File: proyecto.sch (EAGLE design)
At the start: 0 parts

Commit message: Avance :)
.
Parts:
- added IC1: ADE9153AACPZ, SamacSys_Parts:ADE9153AACPZ
- added J1: 796638-3, SamacSys_Parts:796638-3
- added K1: PR28-3V-360-1A-E, PR28-3V-360-1A-E:PR28-3V-360-1A-E
- added PS1: RAC03-3.3SK, SamacSys_Parts:RAC03-3.3SK
- added U1: ESP32-PICO-MINI-02-N8R2ESP32-PICO-MINI-02_EXP, 2024-09-07_16-09-34_Library:ESP32-PICO-MINI-02-N8R2ESP32-PICO-MINI-02_EXP
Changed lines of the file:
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@@
 <setting verticaltext="up"/>
 </settings>
-<grid distance="0.1" unitdist="inch" unit="inch" style="lines" multiple="1" display="yes" altdistance="0.01" altunitdist="inch" altunit="inch"/>
+<grid distance="0.1" unitdist="inch" unit="inch" style="lines" multiple="1" display="no" altdistance="0.01" altunitdist="inch" altunit="inch"/>
 <layers>
+<layer number="1" name="Top" color="4" fill="1" visible="no" active="no"/>
+<layer number="2" name="Route2" color="1" fill="3" visible="no" active="no"/>
+<layer number="3" name="Route3" color="4" fill="3" visible="no" active="no"/>
+<layer number="4" name="Route4" color="1" fill="4" visible="no" active="no"/>
+<layer number="5" name="Route5" color="4" fill="4" visible="no" active="no"/>
+<layer number="6" name="Route6" color="1" fill="8" visible="no" active="no"/>
+<layer number="7" name="Route7" color="4" fill="8" visible="no" active="no"/>
+<layer number="8" name="Route8" color="1" fill="2" visible="no" active="no"/>
+<layer number="9" name="Route9" color="4" fill="2" visible="no" active="no"/>
+<layer number="10" name="Route10" color="1" fill="7" visible="no" active="no"/>
+<layer number="11" name="Route11" color="4" fill="7" visible="no" active="no"/>
+<layer number="12" name="Route12" color="1" fill="5" visible="no" active="no"/>
+<layer number="13" name="Route13" color="4" fill="5" visible="no" active="no"/>
+<layer number="14" name="Route14" color="1" fill="6" visible="no" active="no"/>
+<layer number="15" name="Route15" color="4" fill="6" visible="no" active="no"/>
+<layer number="16" name="Bottom" color="1" fill="1" visible="no" active="no"/>
+<layer number="17" name="Pads" color="2" fill="1" visible="no" active="no"/>
+<layer number="18" name="Vias" color="2" fill="1" visible="no" active="no"/>
+<layer number="19" name="Unrouted" color="6" fill="1" visible="no" active="no"/>
+<layer number="20" name="Dimension" color="15" fill="1" visible="no" active="no"/>
+<layer number="21" name="tPlace" color="7" fill="1" visible="no" active="no"/>
+<layer number="22" name="bPlace" color="7" fill="1" visible="no" active="no"/>
+<layer number="23" name="tOrigins" color="15" fill="1" visible="no" active="no"/>
+<layer number="24" name="bOrigins" color="15" fill="1" visible="no" active="no"/>
+<layer number="25" name="tNames" color="7" fill="1" visible="no" active="no"/>
+<layer number="26" name="bNames" color="7" fill="1" visible="no" active="no"/>
+<layer number="27" name="tValues" color="7" fill="1" visible="no" active="no"/>
+<layer number="28" name="bValues" color="7" fill="1" visible="no" active="no"/>
+<layer number="29" name="tStop" color="7" fill="3" visible="no" active="no"/>
+<layer number="30" name="bStop" color="7" fill="6" visible="no" active="no"/>
+<layer number="31" name="tCream" color="7" fill="4" visible="no" active="no"/>
+<layer number="32" name="bCream" color="7" fill="5" visible="no" active="no"/>
+<layer number="33" name="tFinish" color="6" fill="3" visible="no" active="no"/>
+<layer number="34" name="bFinish" color="6" fill="6" visible="no" active="no"/>
+<layer number="35" name="tGlue" color="7" fill="4" visible="no" active="no"/>
+<layer number="36" name="bGlue" color="7" fill="5" visible="no" active="no"/>
+<layer number="37" name="tTest" color="7" fill="1" visible="no" active="no"/>
+<layer number="38" name="bTest" color="7" fill="1" visible="no" active="no"/>
+<layer number="39" name="tKeepout" color="4" fill="11" visible="no" active="no"/>
+<layer number="40" name="bKeepout" color="1" fill="11" visible="no" active="no"/>
+<layer number="41" name="tRestrict" color="4" fill="10" visible="no" active="no"/>
+<layer number="42" name="bRestrict" color="1" fill="10" visible="no" active="no"/>
+<layer number="43" name="vRestrict" color="2" fill="10" visible="no" active="no"/>
+<layer number="44" name="Drills" color="7" fill="1" visible="no" active="no"/>
+<layer number="45" name="Holes" color="7" fill="1" visible="no" active="no"/>
+<layer number="46" name="Milling" color="3" fill="1" visible="no" active="no"/>
+<layer number="47" name="Measures" color="7" fill="1" visible="no" active="no"/>
+<layer number="48" name="Document" color="7" fill="1" visible="no" active="no"/>
+<layer number="49" name="Reference" color="7" fill="1" visible="no" active="no"/>
+<layer number="51" name="tDocu" color="7" fill="1" visible="no" active="no"/>
+<layer number="52" name="bDocu" color="7" fill="1" visible="no" active="no"/>
 <layer number="88" name="SimResults" color="9" fill="1" visible="yes" active="yes"/>
 <layer number="89" name="SimProbes" color="9" fill="1" visible="yes" active="yes"/>
@@
 <parts>
 <part name="FRAME1" library="frames" library_urn="urn:adsk.eagle:library:229" deviceset="A4L-LOC" device=""/>
+<part name="J1" library="SamacSys_Parts" deviceset="796638-3" device=""/>
+<part name="PS1" library="SamacSys_Parts" deviceset="RAC03-3.3SK" device=""/>
+<part name="K1" library="PR28-3V-360-1A-E" deviceset="PR28-3V-360-1A-E" device=""/>
+<part name="FRAME2" library="frames" library_urn="urn:adsk.eagle:library:229" deviceset="A4L-LOC" device=""/>
+<part name="U1" library="2024-09-07_16-09-34_Library" deviceset="ESP32-PICO-MINI-02-N8R2" device="ESP32-PICO-MINI-02_EXP"/>
+<part name="IC1" library="SamacSys_Parts" deviceset="ADE9153AACPZ" device=""/>
 </parts>
 <sheets>
@@
 <attribute name="SHEET" x="230.505" y="5.08" size="2.54" layer="94"/>
 </instance>
+<instance part="J1" gate="G$1" x="33.02" y="149.86" smashed="yes">
+<attribute name="NAME" x="49.53" y="157.48" size="1.778" layer="95" align="center-left"/>
+<attribute name="VALUE" x="49.53" y="154.94" size="1.778" layer="96" align="center-left"/>
+</instance>
+<instance part="PS1" gate="G$1" x="27.94" y="116.84" smashed="yes">
+<attribute name="NAME" x="62.23" y="124.46" size="1.778" layer="95" align="center-left"/>
+<attribute name="VALUE" x="62.23" y="121.92" size="1.778" layer="96" align="center-left"/>
+</instance>
+<instance part="K1" gate="G$1" x="363.22" y="121.92" smashed="yes">
+<attribute name="NAME" x="355.6" y="128.27" size="1.778" layer="95"/>
+<attribute name="VALUE" x="355.6" y="114.3" size="1.778" layer="96"/>
+</instance>
+<instance part="FRAME2" gate="G$1" x="269.24" y="0" smashed="yes">
+<attribute name="DRAWING_NAME" x="486.41" y="15.24" size="2.54" layer="94"/>
+<attribute name="LAST_DATE_TIME" x="486.41" y="10.16" size="2.286" layer="94"/>
+<attribute name="SHEET" x="499.745" y="5.08" size="2.54" layer="94"/>
+</instance>
+<instance part="U1" gate="A" x="109.22" y="142.24" smashed="yes">
+<attribute name="NAME" x="124.8146" y="151.3586" size="2.083" layer="95" ratio="6"/>
+<attribute name="VALUE" x="124.1752" y="148.8186" size="2.083" layer="96" ratio="6"/>
+</instance>
+<instance part="IC1" gate="G$1" x="401.32" y="106.68" smashed="yes">
+<attribute name="NAME" x="433.07" y="134.62" size="1.778" layer="95" align="center-left"/>
+<attribute name="VALUE" x="433.07" y="132.08" size="1.778" layer="96" align="center-left"/>
+</instance>
 </instances>

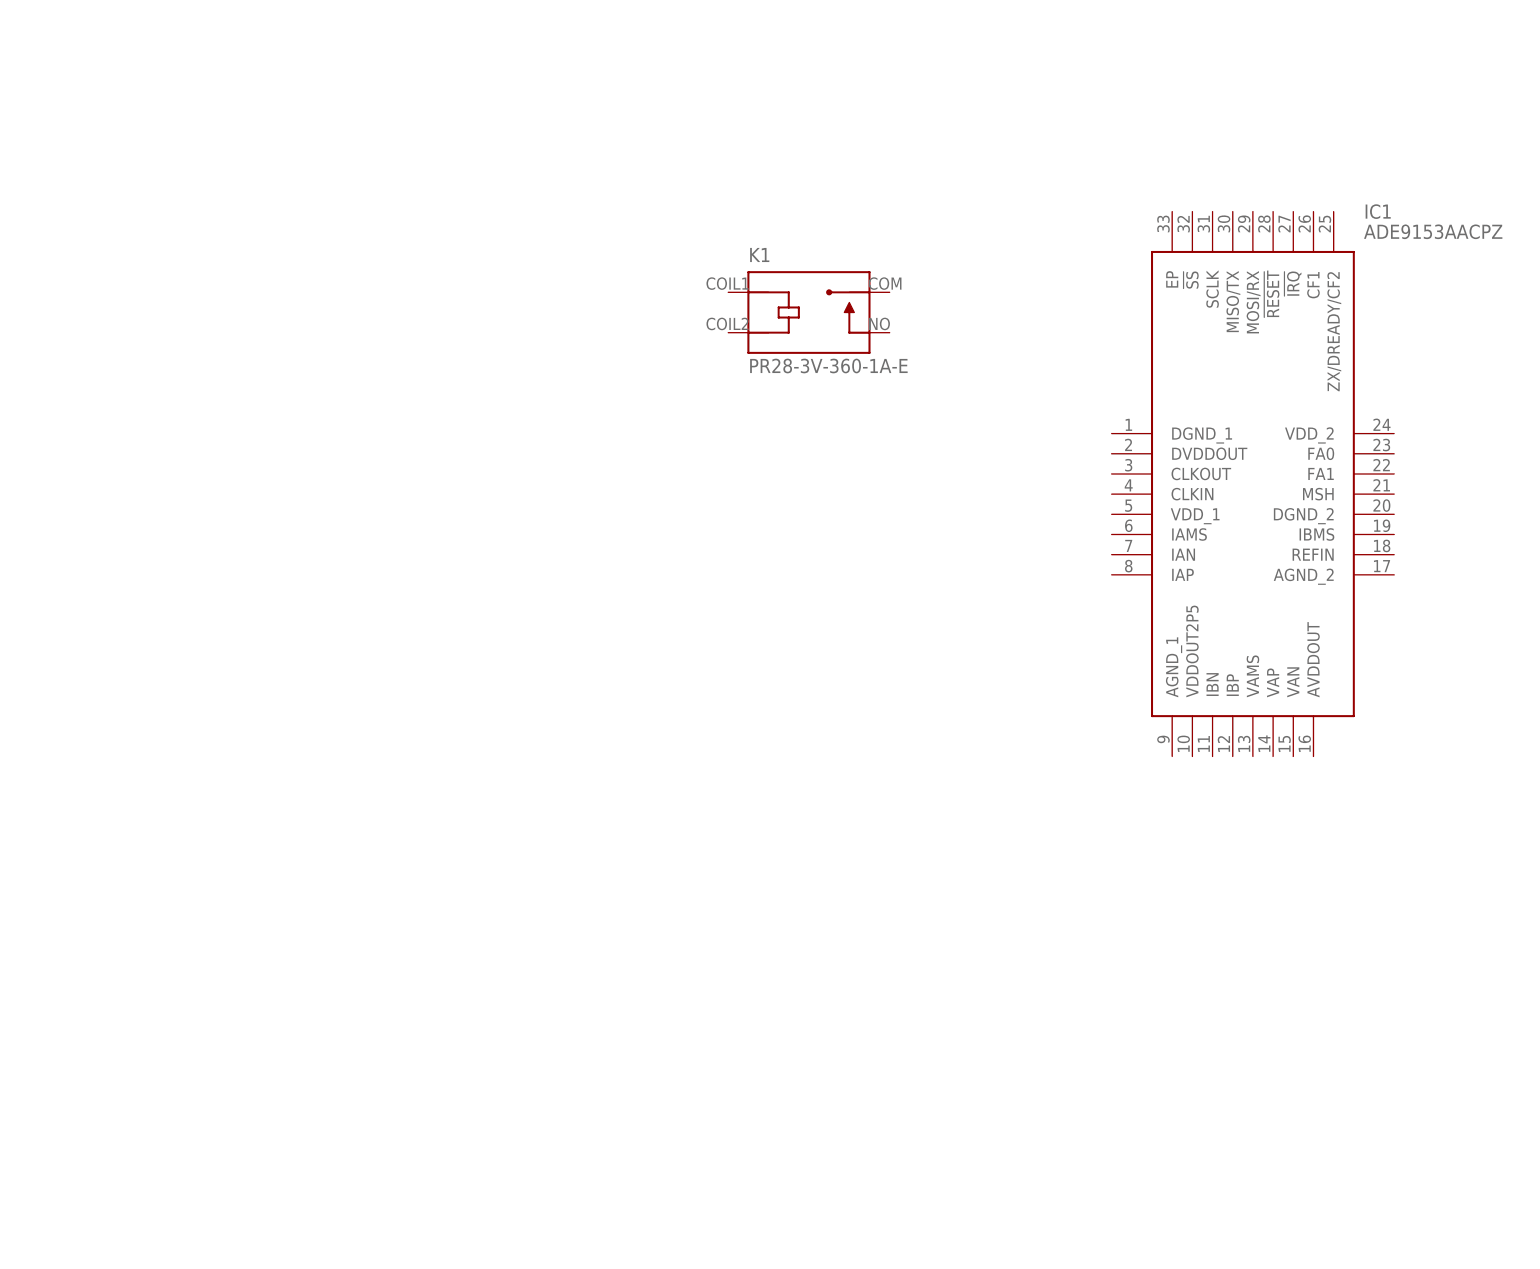
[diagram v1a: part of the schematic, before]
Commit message: Condensadores de acople del integrado de medicion de energia
Se añadio algunos condensadores de acople que se especifico en la hoja de datos del medidor de energia y el oscilador que se especifica.
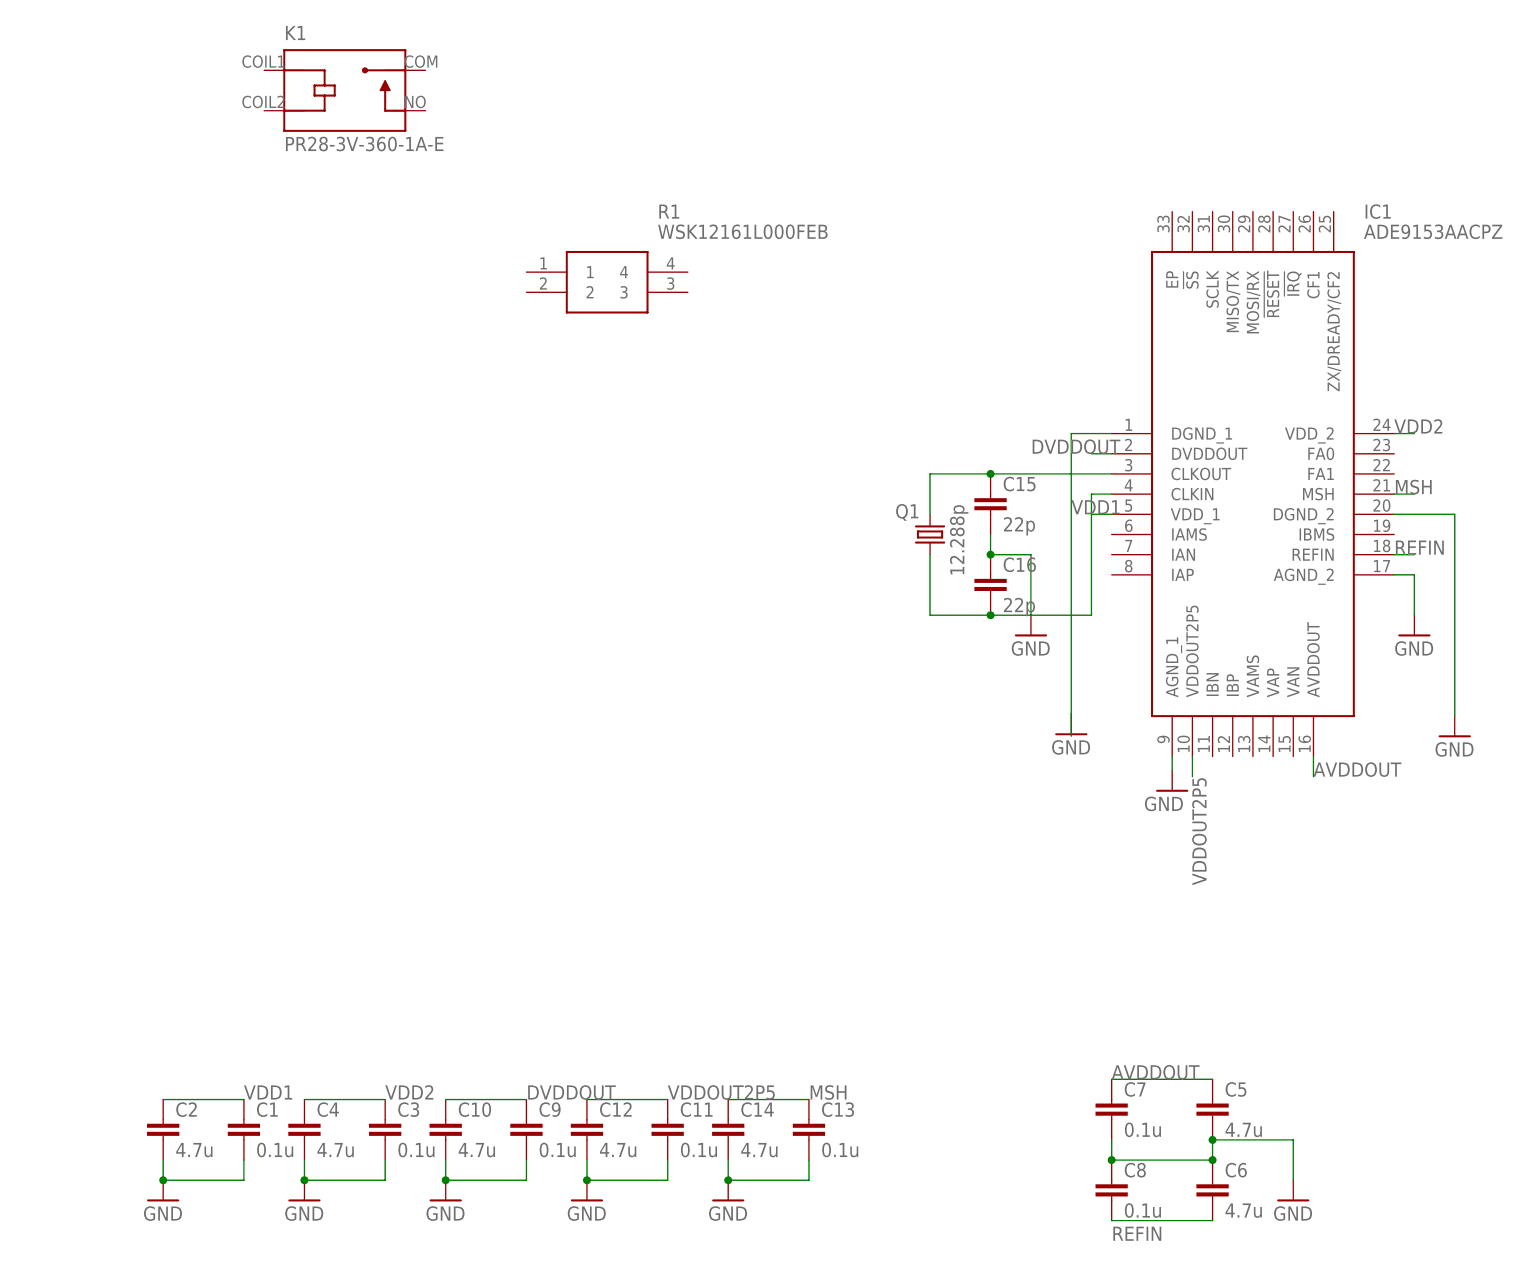
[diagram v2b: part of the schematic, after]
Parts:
- added C1, C11, C13, C3, C7, C8, C9: 0.1u, rcl:C-EUC0201
- added C10, C12, C14, C2, C4, C5, C6: 4.7u, rcl:C-EUC0201
- added C15, C16: 22p, rcl:C-EUC0201
- added Q1: 12.288p, crystal-geyer_V1_0:KX-5
- added R1: WSK12161L000FEB, SamacSys_Parts:WSK12161L000FEB
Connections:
- new net AVDDOUT: C5.1, C7.1, IC1.AVDDOUT
- new net DVDDOUT: C10.1, C9.1, IC1.DVDDOUT
- new net GND: C1.2, C10.2, C11.2, C12.2, C13.2, C14.2, C15.2, C16.1, C2.2, C3.2, C4.2, C5.2, C6.1, C7.2, C8.1, C9.2, IC1.AGND_1, IC1.AGND_2, IC1.DGND_1, IC1.DGND_2
- new net MSH: C13.1, C14.1, IC1.MSH
- new net N$2: C15.1, IC1.CLKOUT, Q1.2
- new net N$3: C16.2, IC1.CLKIN, Q1.1
- new net REFIN: C6.2, C8.2, IC1.REFIN
- new net VDD1: C1.1, C2.1, IC1.VDD_1
- new net VDD2: C3.1, C4.1, IC1.VDD_2
- new net VDDOUT2P5: C11.1, C12.1, IC1.VDDOUT2P5
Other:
- moved on the sheet: K1

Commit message: Conexiones según fabricante
Se realizaron algunas conexiones de los condensadores de acople recomendados por el fabricante, se conecto tambien la resistencia Shunt y su filtro de antialising. Ademas se añadieron las resistencias para el sensado del voltaje.

Por ultimo se añadio los condensadores de acople del ESP32
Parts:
- added C17: 0.47u, rcl:C-EUC0201
- added C18, C19, C22: 0.1u, rcl:C-EUC0201
- added C20: 0.15u, rcl:C-EUC0201
- added C21: 22u, rcl:C-EUC0201
- added R2: 150k, rcl:R-US_R0201
- added R3: WSK12161L000FEB, SamacSys_Parts:WSK12161L000FEB
- added R4, R5, R6: 330k, rcl:R-US_R0603
- added R7: 1k, rcl:R-US_R0603
- Q1: value 12.288p -> 12.288M
- R1: value WSK12161L000FEB -> 150k; device SamacSys_Parts:WSK12161L000FEB -> rcl:R-US_R0201
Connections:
- net N$2 renamed CLKOUT
- net N$3 renamed CLKIN
- new net +3V3: C21.1, C22.1, PS1.+VOUT, U1.3V3
- new net N$1: C17.1, IC1.FA0
- new net N$10: C20.1, IC1.VAMS, IC1.VAN, R7.2
- new net N$2: R1.1, R3.3
- new net N$3: C18.1, IC1.IAN, R1.2
- new net N$4: C17.2, IC1.FA1
- new net N$5: C19.2, IC1.IAP, R2.2
- new net N$6: R2.1, R3.2
- new net N$7: R4.2, R5.1
- new net N$8: R5.2, R6.1
- new net N$9: C20.2, IC1.VAP, R6.2, R7.1
- net GND: now also C18.2, C19.1, C21.2, C22.2, PS1.-VOUT
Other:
- moved on the sheet: C15, C16, PS1, Q1
